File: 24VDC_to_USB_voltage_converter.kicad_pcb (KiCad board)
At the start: 2 copper layers, 60 x 26 mm, 33 parts, among them J1 Conn_01x02, J2 USB_A, J3 Conn_01x02, Q1 CPH6341-TL-W, U1 TPS54308

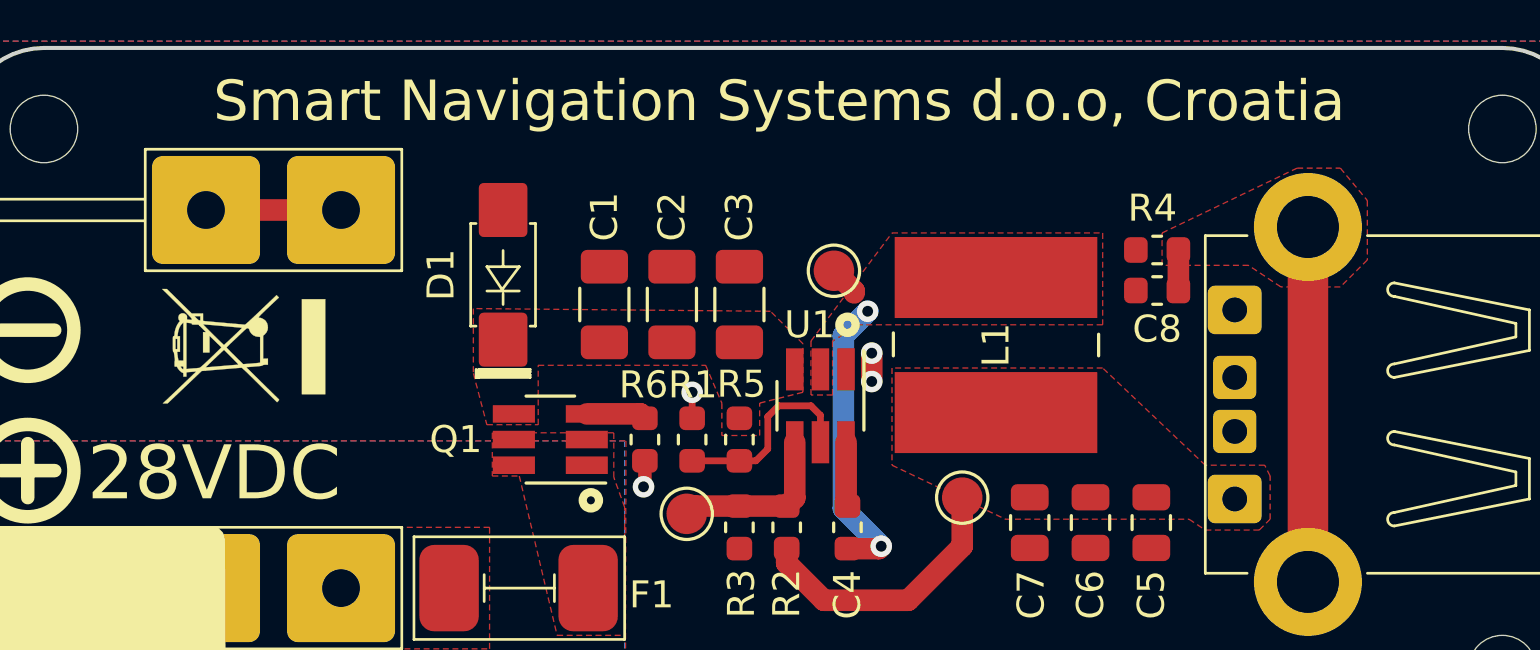
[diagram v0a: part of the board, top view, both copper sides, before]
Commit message: Adding final changes and exporting Gerbers
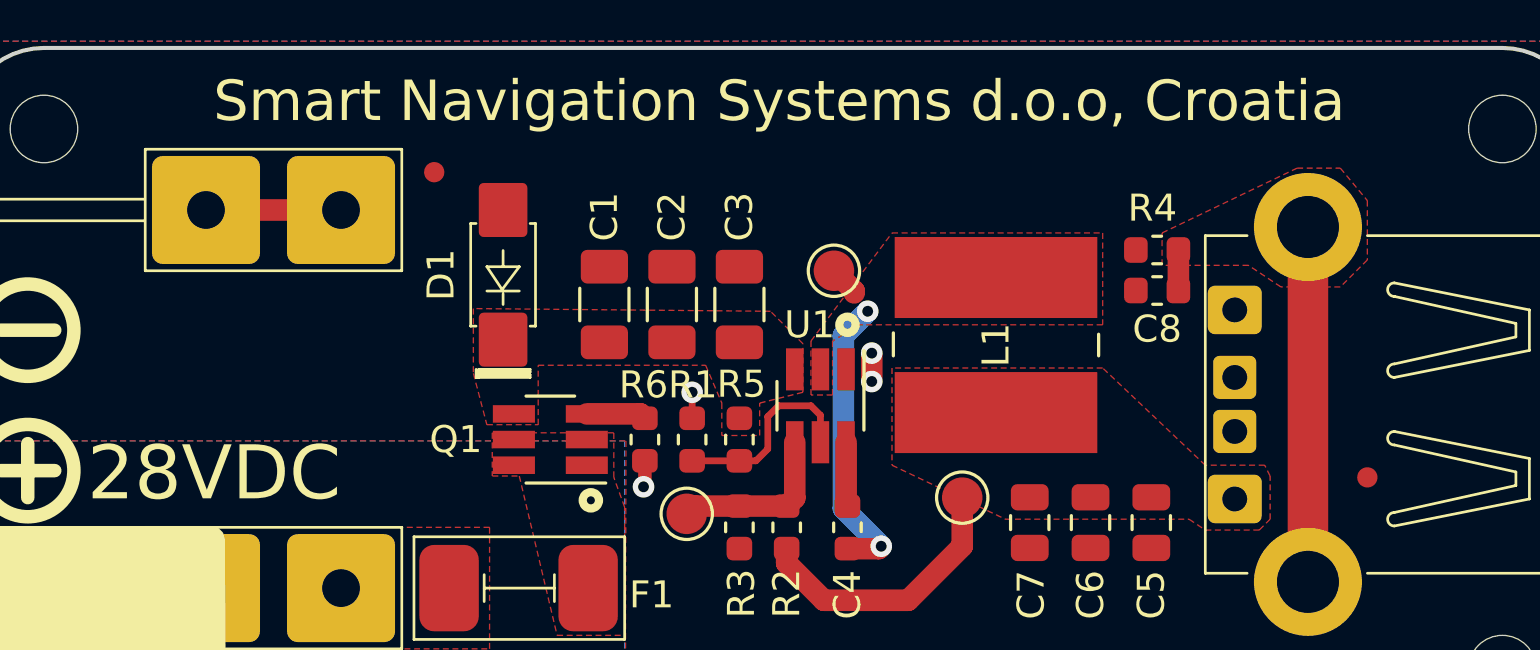
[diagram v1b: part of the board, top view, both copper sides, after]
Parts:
- removed G***: LOGO, footprints:magniblu_logo
- removed REF**: CE-Logo_8.5x6mm_SilkScreen, Symbol:CE-Logo_8.5x6mm_SilkScreen
- removed REF**: RoHS-Logo_6mm_SilkScreen, Symbol:RoHS-Logo_6mm_SilkScreen
- removed REF**: WEEE-Logo_4.2x6mm_SilkScreen, Symbol:WEEE-Logo_4.2x6mm_SilkScreen
- added FID1: FIDUCIAL, Fiducial:Fiducial_0.75mm_Dia_1.5mm_Outer, F.Cu at (157.0, 90.7)
- added FID2: FIDUCIAL, Fiducial:Fiducial_0.75mm_Dia_1.5mm_Outer, F.Cu at (122.5, 79.3)

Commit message: Finishing the board and creating gerbers for ordering
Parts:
- FID1, FID2: footprint Fiducial:Fiducial_0.75mm_Dia_1.5mm_Outer -> footprints:FIDUCIAL
- moved FID2 96.2 mm to (37.2, 34.8)
- moved C5 96.1 mm to (67.2, 41.9)
- moved C6 96.1 mm to (65.0, 41.9)
- moved C7 96.1 mm to (62.7, 41.9)
- moved J2 96.1 mm to (70.2, 37.5)
- moved TP2 96.1 mm to (50.0, 41.6)
- moved C1 96.1 mm to (47.0, 33.9)
- moved C2 96.1 mm to (49.5, 33.9)
- moved C3 96.1 mm to (52.0, 33.9)
- moved C4 96.1 mm to (56.0, 42.1)
- moved C8 96.1 mm to (67.4, 33.3)
- moved D1 96.1 mm to (43.2, 32.9)
- moved F1 96.1 mm to (41.2, 44.4)
- moved J1 96.1 mm to (34.7, 44.4)
- moved J3 96.1 mm to (34.7, 30.4)
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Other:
- board text added: "9-28VDC 0.8A input / output 5.0V 1.0A"
- board text added: "FB"
- board text added: "SW"
- board text added: "VBUS"
- board text removed: "9-28VDC 1.2A input / output 5.0V 1.0A"

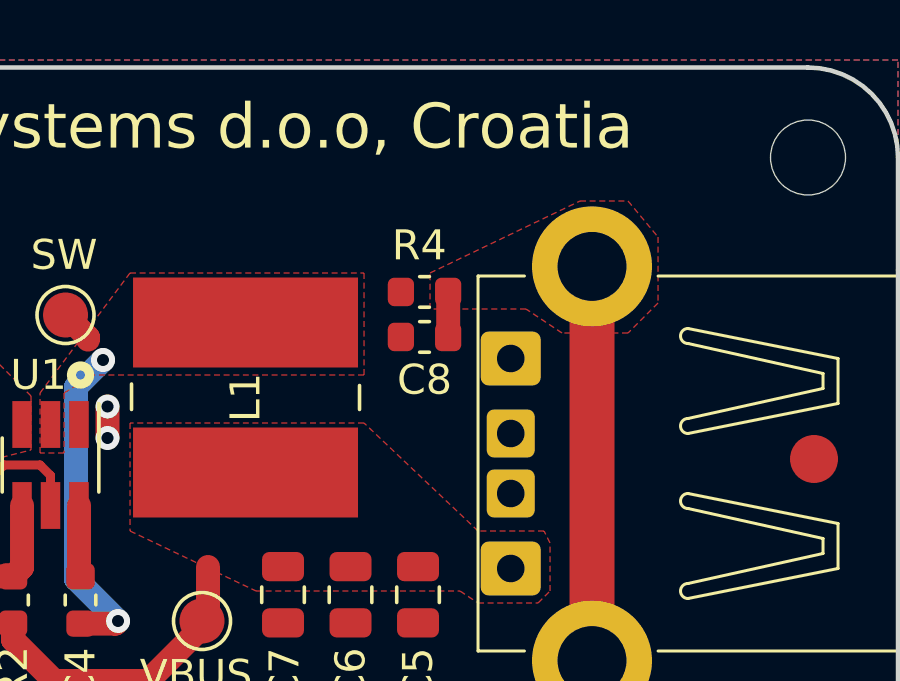
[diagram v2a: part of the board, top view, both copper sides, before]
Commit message: Adding short resistor between d+ and d-, small changes in PCB
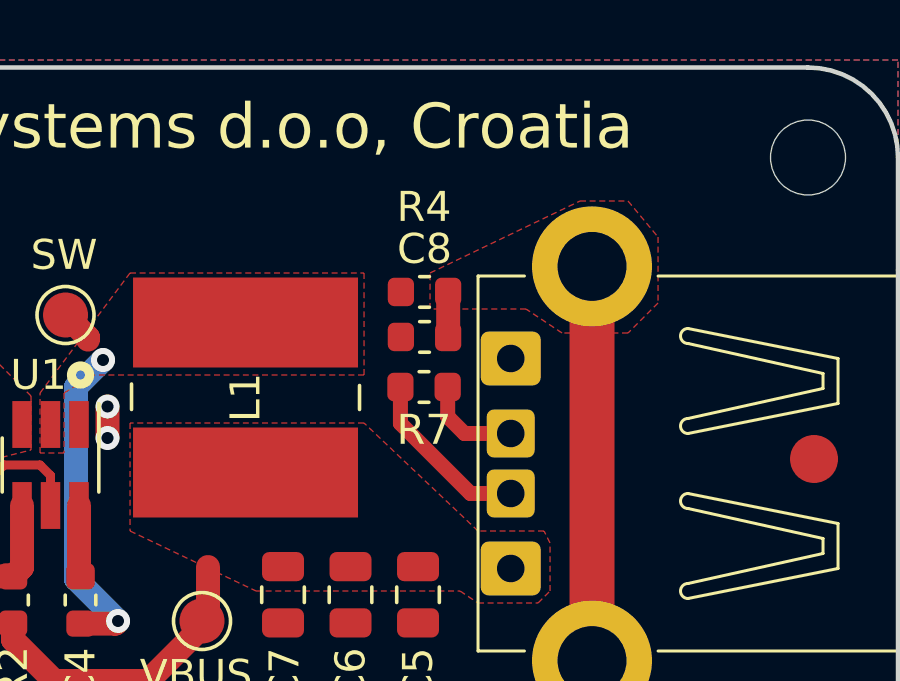
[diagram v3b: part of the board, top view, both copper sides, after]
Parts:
- added R7: 0R, Resistor_SMD:R_0603_1608Metric, F.Cu at (67.4, 35.0)
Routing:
- net Net-(J2-Pad2): track 0.00 -> 5.86 mm
- net Net-(J2-Pad3): track 0.00 -> 3.32 mm
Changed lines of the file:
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@@
     (thickness 1.6)
     (drawings 27)
-    (tracks 42)
+    (tracks 49)
     (zones 0)
-    (modules 31)
+    (modules 32)
     (nets 14)
   )
@@
     (uvia_drill 0.1)
   )
+  (module Resistor_SMD:R_0603_1608Metric (layer F.Cu)
+    (at 67.4 35 180)
+    (descr "Resistor SMD 0603 (1608 Metric), square (rectangular) end terminal, IPC_7351 nominal, (Body size source: http://www.tortai-tech.com/upload/download/2011102023233369053.pdf), generated with kicad-footprint-generator")
+    (tags resistor)
+    (attr smd)
+    (fp_text reference R7 (at 0 -1.43 180) (layer F.SilkS)
+      (effects (font (size 1 1) (thickness 0.15)))
+    )
+    (fp_text value 0R (at 0 1.43 180) (layer F.Fab)
+      (effects (font (size 1 1) (thickness 0.15)))
+    )
+    (fp_line (start -0.8 0.4) (end -0.8 -0.4) (layer F.Fab) (width 0.1))
+    (fp_line (start -0.8 -0.4) (end 0.8 -0.4) (layer F.Fab) (width 0.1))
+    (fp_line (start 0.8 -0.4) (end 0.8 0.4) (layer F.Fab) (width 0.1))
+    (fp_line (start 0.8 0.4) (end -0.8 0.4) (layer F.Fab) (width 0.1))
+    (fp_line (start -0.162779 -0.51) (end 0.162779 -0.51) (layer F.SilkS) (width 0.12))
+    (fp_line (start -0.162779 0.51) (end 0.162779 0.51) (layer F.SilkS) (width 0.12))
+    (fp_line (start -1.48 0.73) (end -1.48 -0.73) (layer F.CrtYd) (width 0.05))
+    (fp_line (start -1.48 -0.73) (end 1.48 -0.73) (layer F.CrtYd) (width 0.05))
+    (fp_line (start 1.48 -0.73) (end 1.48 0.73) (layer F.CrtYd) (width 0.05))
+    (fp_line (start 1.48 0.73) (end -1.48 0.73) (layer F.CrtYd) (width 0.05))
+    (fp_text user %R (at 0 0 180) (layer F.Fab)
+      (effects (font (size 0.4 0.4) (thickness 0.06)))
+    )
+    (pad 1 smd roundrect (at -0.7875 0 180) (size 0.875 0.95) (layers F.Cu F.Paste F.Mask) (roundrect_rratio 0.25)
+      (net 10 "Net-(J2-Pad3)"))
+    (pad 2 smd roundrect (at 0.7875 0 180) (size 0.875 0.95) (layers F.Cu F.Paste F.Mask) (roundrect_rratio 0.25)
+      (net 9 "Net-(J2-Pad2)"))
+    (model ${KISYS3DMOD}/Resistor_SMD.3dshapes/R_0603_1608Metric.wrl
+      (at (xyz 0 0 0))
+      (scale (xyz 1 1 1))
+      (rotate (xyz 0 0 0))
+    )
+  )
   (module footprints:FIDUCIAL (layer F.Cu)
     (at 37.2 34.8)
@@
     (tags capacitor)
     (attr smd)
-    (fp_text reference C8 (at 0 -1.43 180) (layer F.SilkS)
+    (fp_text reference C8 (at 0 2.931307 180) (layer F.SilkS)
       (effects (font (size 1 1) (thickness 0.15)))
     )
@@
     (tags resistor)
     (attr smd)
-    (fp_text reference R4 (at 0.175 1.55 180) (layer F.SilkS)
+    (fp_text reference R4 (at 0.016808 2.831307 180) (layer F.SilkS)
       (effects (font (size 1 1) (thickness 0.15)))
     )
@@
   (segment (start 55.9 41.2625) (end 55.95 41.3125) (width 0.8) (layer F.Cu) (net 7))
   (segment (start 55.9 38.95) (end 55.9 41.2625) (width 0.8) (layer F.Cu) (net 7))
+  (segment (start 68.95 38.55) (end 70.29 38.55) (width 0.5) (layer F.Cu) (net 9))
+  (segment (start 66.6125 36.2125) (end 68.95 38.55) (width 0.5) (layer F.Cu) (net 9))
+  (segment (start 66.6125 35) (end 66.6125 36.2125) (width 0.5) (layer F.Cu) (net 9))
+  (segment (start 68.75 36.55) (end 69.39 36.55) (width 0.5) (layer F.Cu) (net 10))
+  (segment (start 68.1875 35.9875) (end 68.75 36.55) (width 0.5) (layer F.Cu) (net 10))
+  (segment (start 69.39 36.55) (end 70.29 36.55) (width 0.5) (layer F.Cu) (net 10))
+  (segment (start 68.1875 35) (end 68.1875 35.9875) (width 0.5) (layer F.Cu) (net 10))
   (segment (start 50.2 39.6375) (end 51.95 39.6375) (width 0.4) (layer F.Cu) (net 11))
   (segment (start 52.5625 39.6375) (end 51.95 39.6375) (width 0.3) (layer F.Cu) (net 11))
@@
       )
     )
+  )
+  (zone (net 0) (net_name "") (layer F.Cu) (hatch edge 0.508)
+    (connect_pads yes (clearance 0.25))
+    (min_thickness 0.25)
+    (keepout (tracks allowed) (vias allowed) (copperpour not_allowed))
+    (fill (arc_segments 16) (thermal_gap 0.508) (thermal_bridge_width 0.508))
+    (polygon
+      (pts
+        (xy 57.6 34.6) (xy 57.6 36) (xy 65.8 36) (xy 65.8 34.6)
+      )
+    )
